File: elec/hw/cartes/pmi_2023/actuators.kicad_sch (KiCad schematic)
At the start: 0 parts

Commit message: pmi 2023 wip
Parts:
- added C27, C29, C30, C31, C32, C33, C34, C35, C36: 100nF 50V, symbol cocotter_capacitors:C_100nF_50V_0603
- added C28: 10µF 16V, symbol cocotter_capacitors:C_10µF_16V_0805
- added D2: green, 0603, symbol cocotter_diodes:green_led_0603
- added D3: yellow, 0603, symbol cocotter_diodes:yellow_led_0603
- added D4: red, 0603, symbol cocotter_diodes:red_led_0603
- added R49, R50, R51: 1k 1%, cocotter_resistor:r0603_reflow, symbol cocotter_resistors:R_1k_0603_1%
- added R87, R88, R89, R90, R91, R92, R93, R94: 0R, cocotter_resistor:r0603_reflow, symbol cocotter_resistors:R_0R_0603
- added U28: PCA9685PW, Package_SO:TSSOP-28_4.4x9.7mm_P0.65mm, symbol cocotter_ic:PCA9685PW
- added U29, U30, U31, U32: SN74LVC1T45DBV, Package_TO_SOT_SMD:SOT-23-6, symbol cocotter_ic:SN74LVC1T45DBV
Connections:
- new net: R92.2, U28.1 (A0)
- new net: R89.1, U28.2 (A1)
- new net: R94.2, U28.24 (A5)
- new net: R88.1, U28.25 (EXTCLK)
- new net: R90.1, U28.3 (A2)
- new net: R93.2, U28.4 (A3)
- new net: R91.1, U28.5 (A4)
- new net: D2.2 (A), R49.2
- new net: D4.2 (A), R51.2
- new net: D3.2 (A), R50.2
- new net +3V3: C27.1, C28.1, C29.1, C31.1, C33.1, C35.1, R49.1, R50.1, R51.1, R92.1, R93.1, R94.1, U28.28 (VDD), U29.1 (VCCA), U29.5 (DIR), U30.1 (VCCA), U30.5 (DIR), U31.1 (VCCA), U31.5 (DIR), U32.1 (VCCA), U32.5 (DIR)
- new net +5V: C30.1, C32.1, C34.1, C36.1, U29.6 (VCCB), U30.6 (VCCB), U31.6 (VCCB), U32.6 (VCCB)
- new net GND: C27.2, C28.2, C29.2, C30.2, C31.2, C32.2, C33.2, C34.2, C35.2, C36.2, R87.2, R88.2, R89.2, R90.2, R91.2, U28.14 (VSS), U29.2 (GND), U30.2 (GND), U31.2 (GND), U32.2 (GND)
- new net LED_RGB_B_3v3: U28.21 (LED14)
- new net LED_RGB_G_3v3: U28.20 (LED13)
- new net LED_RGB_R_3v3: U28.19 (LED12)
- new net LED_RGB_W_3v3: U28.22 (LED15)
- new net enable_tof_3v3: U28.13 (LED7)
- new net led_vbatt_error: D4.1 (K), U28.18 (LED11)
- new net led_vbatt_ok: D2.1 (K), U28.16 (LED9)
- new net led_vbatt_warning: D3.1 (K), U28.17 (LED10)
- new net line_led_pwm_3v3: U28.15 (LED8)
- new net scl_3v3: U28.26 (SCL)
- new net sda_3v3: U28.27 (SDA)
- new net servo_pwm_0_3v3: U28.6 (LED0), U29.3 (A)
- new net servo_pwm_0_5V: U29.4 (B)
- new net servo_pwm_1_3v3: U28.7 (LED1)
- new net servo_pwm_1_5V: U30.4 (B)
- new net servo_pwm_2_3v3: U28.8 (LED2)
- new net servo_pwm_2_5V: U31.4 (B)
- new net servo_pwm_3_3v3: U28.9 (LED3), U32.3 (A)
- new net servo_pwm_3_5V: U32.4 (B)
- new net servos_nOE: R87.1, U28.23 (~{OE})
- new net /reset_tof_3v3: U28.12 (LED6)

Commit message: pmi2023 wip
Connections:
- net pwm_vaccum_3v3: now reaches U28.11 (LED5)
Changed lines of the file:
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@@
+    (stroke (width 0) (type default))
+  )
+  (wire (pts (xy 113.03 49.53) (xy 97.79 49.53))
     (stroke (width 0) (type default))
   )
@@
     (effects (font (size 1.27 1.27)) (justify left))
   )
+  (hierarchical_label "pwm_vaccum_3v3" (shape output) (at 113.03 49.53 0) (fields_autoplaced)
+    (effects (font (size 1.27 1.27)) (justify left))
+  )

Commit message: pmi2023 wip
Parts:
- added C43 (x4): 10µF 16V, symbol cocotter_capacitors:C_10µF_16V_0805
- added J3 (x4): con_servo, symbol cocotter_connectors:con_servo
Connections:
- net +5V: now also C43.1, C43.1, C43.1, C43.1, J3.2 (5V), J3.2 (5V), J3.2 (5V), J3.2 (5V)
- net GND: now also C43.2, C43.2, C43.2, C43.2, J3.1 (GND), J3.1 (GND), J3.1 (GND), J3.1 (GND)
- net servo_pwm_0_5V: now also J3.3 (PWM)
- net servo_pwm_1_3v3: now also U30.3 (A)
- net servo_pwm_1_5V: now also J3.3 (PWM)
- net servo_pwm_2_3v3: now also U31.3 (A)
- net servo_pwm_2_5V: now also J3.3 (PWM)
- net servo_pwm_3_5V: now also J3.3 (PWM)

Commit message: pmi_2023 wip
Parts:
- C27, C29, C30, C31, C32, C33, C34, C35, C36: footprint (none) -> cocotter_capacitors:C_0603_1608Metric
- C28, C43: footprint (none) -> cocotter_capacitors:C_0805_2012Metric
- D2, D3, D4: footprint (none) -> cocotter_diodes:LED_0603_1608Metric
- J3: footprint (none) -> cocotter_connectors:ana_servo_5V
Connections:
- net led_vbatt_error: now also D4.c; no longer D4.1 (K)
- net led_vbatt_ok: now also D2.c (C); no longer D2.1 (K)
- net led_vbatt_warning: now also D3.c (C); no longer D3.1 (K)
- net at R49.2: now also D2.a (A); no longer D2.2 (A)
- net at R51.2: now also D4.a (A); no longer D4.2 (A)
- net at R50.2: now also D3.a (A); no longer D3.2 (A)
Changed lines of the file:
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@@
       (effects (font (size 1.27 1.27)) (justify left))
     )
-    (property "Footprint" "" (at 224.4852 64.77 0)
+    (property "Footprint" "cocotter_capacitors:C_0603_1608Metric" (at 224.4852 64.77 0)
       (effects (font (size 1.27 1.27)) hide)
     )
@@
       (effects (font (size 1.27 1.27)) (justify left))
     )
-    (property "Footprint" "" (at 224.4852 27.94 0)
+    (property "Footprint" "cocotter_capacitors:C_0603_1608Metric" (at 224.4852 27.94 0)
       (effects (font (size 1.27 1.27)) hide)
     )
@@
       (effects (font (size 1.27 1.27)) (justify left))
     )
-    (property "Footprint" "" (at 247.3452 48.26 0)
+    (property "Footprint" "cocotter_capacitors:C_0805_2012Metric" (at 247.3452 48.26 0)
       (effects (font (size 1.27 1.27)) hide)
     )
@@
       (effects (font (size 1.27 1.27)) (justify left))
     )
-    (property "Footprint" "" (at 247.3452 160.02 0)
+    (property "Footprint" "cocotter_capacitors:C_0805_2012Metric" (at 247.3452 160.02 0)
       (effects (font (size 1.27 1.27)) hide)
     )
@@
       (effects (font (size 1.27 1.27)))
     )
-    (property "Footprint" "" (at 265.43 114.3 0)
+    (property "Footprint" "cocotter_connectors:ana_servo_5V" (at 265.43 114.3 0)
       (effects (font (size 1.27 1.27)) hide)
     )
@@
         )
         (path "/334a657f-c66c-4260-9567-14f1c99913d7/76b412a5-2e5b-49f9-bfc4-2fef81997c2b"
-          (reference "SERVO02") (unit 1)
+          (reference "SERVO2") (unit 1)
         )
       )
@@
       (effects (font (size 1.27 1.27)) (justify left))
     )
-    (property "Footprint" "" (at 185.1152 27.94 0)
+    (property "Footprint" "cocotter_capacitors:C_0603_1608Metric" (at 185.1152 27.94 0)
       (effects (font (size 1.27 1.27)) hide)
     )
@@
       (effects (font (size 1.27 1.27)))
     )
-    (property "Footprint" "" (at 265.43 77.47 0)
+    (property "Footprint" "cocotter_connectors:ana_servo_5V" (at 265.43 77.47 0)
       (effects (font (size 1.27 1.27)) hide)
     )
@@
       (effects (font (size 1.27 1.27)) (justify left))
     )
-    (property "Footprint" "" (at 185.1152 64.77 0)
+    (property "Footprint" "cocotter_capacitors:C_0603_1608Metric" (at 185.1152 64.77 0)
       (effects (font (size 1.27 1.27)) hide)
     )
@@
       (effects (font (size 1.27 1.27)) (justify left))
     )
-    (property "Footprint" "" (at 185.1152 139.7 0)
+    (property "Footprint" "cocotter_capacitors:C_0603_1608Metric" (at 185.1152 139.7 0)
       (effects (font (size 1.27 1.27)) hide)
     )
@@
       (effects (font (size 1.27 1.27)))
     )
-    (property "Footprint" "" (at 265.43 40.64 0)
+    (property "Footprint" "cocotter_connectors:ana_servo_5V" (at 265.43 40.64 0)
       (effects (font (size 1.27 1.27)) hide)
     )
@@
       (effects (font (size 1.27 1.27)) (justify left))
     )
-    (property "Footprint" "" (at 185.1152 101.6 0)
+    (property "Footprint" "cocotter_capacitors:C_0603_1608Metric" (at 185.1152 101.6 0)
       (effects (font (size 1.27 1.27)) hide)
     )
@@
       (effects (font (size 1.27 1.27)) (justify left))
     )
-    (property "Footprint" "" (at 88.5952 29.21 0)
+    (property "Footprint" "cocotter_capacitors:C_0603_1608Metric" (at 88.5952 29.21 0)
       (effects (font (size 1.27 1.27)) hide)
     )
@@
       (effects (font (size 1.27 1.27)) hide)
     )
-    (property "Footprint" "" (at 160.02 54.61 0)
+    (property "Footprint" "cocotter_diodes:LED_0603_1608Metric" (at 160.02 54.61 0)
       (effects (font (size 1.27 1.27)) hide)
     )
@@
       (effects (font (size 1.27 1.27)) hide)
     )
-    (pin "1")
-    (pin "2")
+    (pin "a")
+    (pin "c")
     (instances
       (project "pmi_2023"
@@
       (effects (font (size 1.27 1.27)) (justify left))
     )
-    (property "Footprint" "" (at 247.3452 121.92 0)
+    (property "Footprint" "cocotter_capacitors:C_0805_2012Metric" (at 247.3452 121.92 0)
       (effects (font (size 1.27 1.27)) hide)
     )
@@
       (effects (font (size 1.27 1.27)))
     )
-    (property "Footprint" "" (at 265.43 152.4 0)
+    (property "Footprint" "cocotter_connectors:ana_servo_5V" (at 265.43 152.4 0)
       (effects (font (size 1.27 1.27)) hide)
     )
@@
       (effects (font (size 1.27 1.27)) (justify left))
     )
-    (property "Footprint" "" (at 224.4852 101.6 0)
+    (property "Footprint" "cocotter_capacitors:C_0603_1608Metric" (at 224.4852 101.6 0)
       (effects (font (size 1.27 1.27)) hide)
     )
@@
       (effects (font (size 1.27 1.27)) (justify left))
     )
-    (property "Footprint" "" (at 247.3452 85.09 0)
+    (property "Footprint" "cocotter_capacitors:C_0805_2012Metric" (at 247.3452 85.09 0)
       (effects (font (size 1.27 1.27)) hide)
     )
@@
       (effects (font (size 1.27 1.27)) (justify left))
     )
-    (property "Footprint" "" (at 106.3752 29.21 0)
+    (property "Footprint" "cocotter_capacitors:C_0805_2012Metric" (at 106.3752 29.21 0)
       (effects (font (size 1.27 1.27)) hide)
     )
@@
       (effects (font (size 1.27 1.27)) hide)
     )
-    (property "Footprint" "" (at 149.86 54.61 0)
+    (property "Footprint" "cocotter_diodes:LED_0603_1608Metric" (at 149.86 54.61 0)
       (effects (font (size 1.27 1.27)) hide)
     )
@@
       (effects (font (size 1.27 1.27)) hide)
     )
-    (pin "1")
-    (pin "2")
+    (pin "a")
+    (pin "c")
     (instances
       (project "pmi_2023"
@@
       (effects (font (size 1.27 1.27)) (justify left))
     )
-    (property "Footprint" "" (at 224.4852 139.7 0)
+    (property "Footprint" "cocotter_capacitors:C_0603_1608Metric" (at 224.4852 139.7 0)
       (effects (font (size 1.27 1.27)) hide)
     )
@@
       (effects (font (size 1.27 1.27)) hide)
     )
-    (property "Footprint" "" (at 139.7 54.61 0)
+    (property "Footprint" "cocotter_diodes:LED_0603_1608Metric" (at 139.7 54.61 0)
       (effects (font (size 1.27 1.27)) hide)
     )
@@
       (effects (font (size 1.27 1.27)) hide)
     )
-    (pin "1")
-    (pin "2")
-    (instances
-      (project "pmi_2023"
+    (pin "a")
+    (pin "c")
+    (instances
+      (project "pmi_2023"

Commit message: wip
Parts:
- removed D2: green, 0603, cocotter_diodes:LED_0603_1608Metric, symbol cocotter_diodes:green_led_0603
- removed D3: yellow, 0603, cocotter_diodes:LED_0603_1608Metric, symbol cocotter_diodes:yellow_led_0603
- removed D4: red, 0603, cocotter_diodes:LED_0603_1608Metric, symbol cocotter_diodes:red_led_0603
- added BATT_LOW1: red, 0603, cocotter_diodes:LED_0603_1608Metric, symbol cocotter_diodes:red_led_0603
- added BATT_OK1: red, 0603, cocotter_diodes:LED_0603_1608Metric, symbol cocotter_diodes:white_led_0603
- added BATT_WARN1: yellow, 0805, cocotter_diodes:LED_0805_2012Metric, symbol cocotter_diodes:yellow_led_0805
- added TP8: TestPoint, cocotter_others:testpoint-THT-0.5mm, symbol cocotter_others:TestPoint
- C13: renamed from C27; JLCPCB (none) -> C14663
- C14: renamed from C28; value 10µF 16V -> 10µF 25V; symbol cocotter_capacitors:C_10µF_16V_0805 -> cocotter_capacitors:C_10µF_16V_0805_X5R; JLCPCB (none) -> C15850; Specification 10µF 16V X7R 0805 -> 10µF 25V X5R 0805
- C15: renamed from C29; JLCPCB (none) -> C14663
- C16: renamed from C31; JLCPCB (none) -> C14663
- C17: renamed from C33; JLCPCB (none) -> C14663
- C18: renamed from C35; JLCPCB (none) -> C14663
- C19: renamed from C30; JLCPCB (none) -> C14663
- C20: renamed from C32; JLCPCB (none) -> C14663
- C21: renamed from C34; JLCPCB (none) -> C14663
- C22: renamed from C36; JLCPCB (none) -> C14663
- C23, C24, C25, C26: renamed from C43; value 10µF 16V -> 10µF 25V; symbol cocotter_capacitors:C_10µF_16V_0805 -> cocotter_capacitors:C_10µF_16V_0805_X5R; JLCPCB (none) -> C15850; Specification 10µF 16V X7R 0805 -> 10µF 25V X5R 0805
- J1, J2, J4: renamed from J3; JLCPCB (none) -> C2932698
- J3: JLCPCB (none) -> C2932698
- R54: renamed from R88; JLCPCB (none) -> C21189
- R55: renamed from R87; JLCPCB (none) -> C21189
- R56: renamed from R89; JLCPCB (none) -> C21189
- R57: renamed from R92; JLCPCB (none) -> C21189
- R58: renamed from R90; JLCPCB (none) -> C21189
- R59: renamed from R93; JLCPCB (none) -> C21189
- R60: renamed from R91; JLCPCB (none) -> C21189
- R61: renamed from R94; JLCPCB (none) -> C21189
- R62: renamed from R49; JLCPCB (none) -> C2991540; mouser 603-RC0603FR-10100KL -> (none)
- R63: renamed from R50; JLCPCB (none) -> C2991540; mouser 603-RC0603FR-10100KL -> (none)
- R64: renamed from R51; JLCPCB (none) -> C2991540; mouser 603-RC0603FR-10100KL -> (none)
- U23: renamed from U28; JLCPCB (none) -> C2678753
- U24: renamed from U29; JLCPCB (none) -> C7843
- U25: renamed from U30; JLCPCB (none) -> C7843
- U26: renamed from U31; JLCPCB (none) -> C7843
- U27: renamed from U32; JLCPCB (none) -> C7843
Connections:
- net led_vbatt_error: now also BATT_LOW1.C
- net led_vbatt_ok: now also BATT_OK1.C
- net led_vbatt_warning: now also BATT_WARN1.C
- net u23_unused_led4: now reaches U23.10 (LED4)
- net u23_unused_led4: now also TP8.1
- net at R62.2: now also BATT_OK1.A
- net at R64.2: now also BATT_LOW1.A
- net at R63.2: now also BATT_WARN1.A
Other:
- moved on the sheet: R62, R64

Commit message: wip
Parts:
- R62, R63, R64: Specification 10k 0603 1% 100mW -> 1k 0603 1% 100mW
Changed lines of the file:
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@@
       (effects (font (size 1.27 1.27)) hide)
     )
-    (property "Specification" "10k 0603 1% 100mW" (at 137.16 46.99 0)
+    (property "Specification" "1k 0603 1% 100mW" (at 137.16 46.99 0)
       (effects (font (size 1.27 1.27)) hide)
     )
@@
       (effects (font (size 1.27 1.27)) hide)
     )
-    (property "Specification" "10k 0603 1% 100mW" (at 149.86 46.99 0)
+    (property "Specification" "1k 0603 1% 100mW" (at 149.86 46.99 0)
       (effects (font (size 1.27 1.27)) hide)
     )
@@
       (effects (font (size 1.27 1.27)) hide)
     )
-    (property "Specification" "10k 0603 1% 100mW" (at 166.37 46.99 0)
-      (effects (font (size 1.27 1.27)) hide)
-    )
+    (property "Specification" "1k 0603 1% 100mW" (at 166.37 46.99 0)
+      (effects (font (size 1.27 1.27)) hide)
+    )

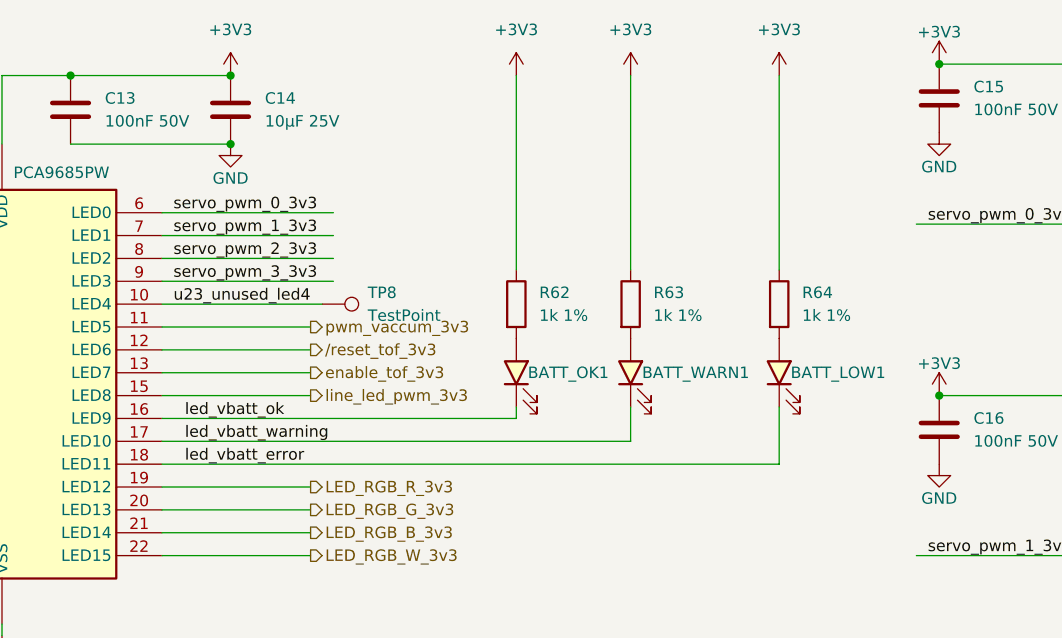
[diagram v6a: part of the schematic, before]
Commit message: pmi layout (WIP)
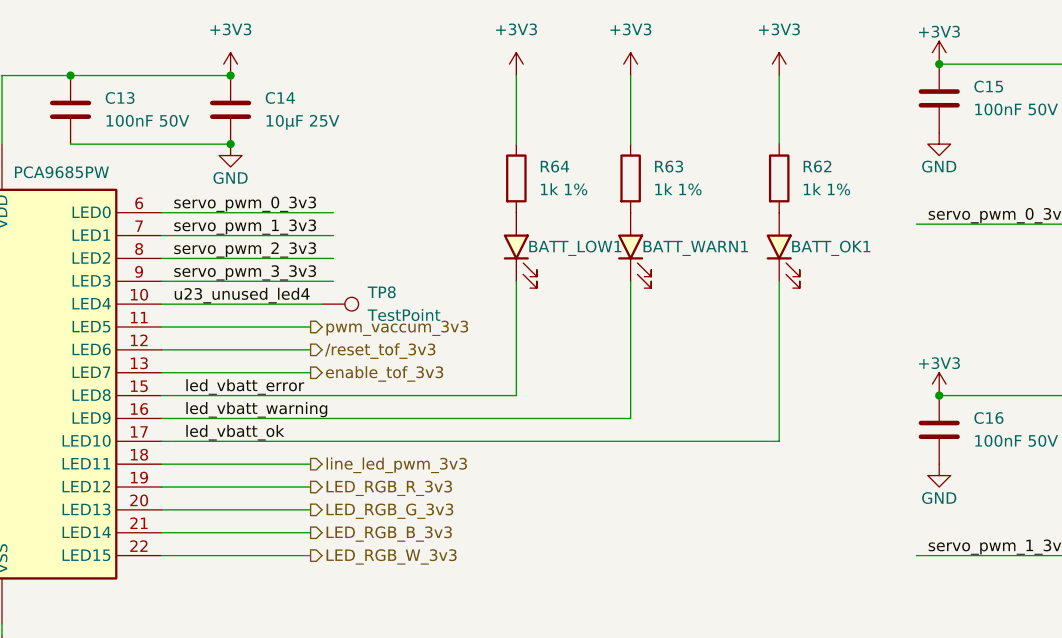
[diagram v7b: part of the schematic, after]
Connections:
- net led_vbatt_error: now also U23.15 (LED8); no longer U23.18 (LED11)
- net led_vbatt_ok: now also U23.17 (LED10); no longer U23.16 (LED9)
- net led_vbatt_warning: now also U23.16 (LED9); no longer U23.17 (LED10)
- net line_led_pwm_3v3: now also U23.18 (LED11); no longer U23.15 (LED8)
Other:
- moved on the sheet: BATT_LOW1, BATT_OK1, BATT_WARN1, R62, R63, R64

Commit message: wip
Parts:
- added D1: ~, cocotter_diodes:3528_PLCC-Reverse_mount, symbol cocotter_diodes:IN-P32TRRRGB
- added R74: 330R 1%, cocotter_resistor:r0603_reflow, symbol cocotter_resistors:R_330R_0603_1%
- added R75, R76: 51R 1%, cocotter_resistor:r0603_reflow, symbol cocotter_resistors:R_51R_0603_1%
- added TP7: TestPoint, cocotter_others:testpoint-THT-0.5mm, symbol cocotter_others:TestPoint
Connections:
- net +3V3: now also D1.4 (COM)
- net LED_RGB_B_3v3 renamed led_RGB_b_3v3
- net led_RGB_b_3v3: now also R75.1
- net LED_RGB_G_3v3 renamed led_RGB_g_3v3
- net led_RGB_g_3v3: now also R76.1
- net LED_RGB_R_3v3 renamed led_RGB_r_3v3
- net led_RGB_r_3v3: now also R74.1
- net LED_RGB_W_3v3 renamed u23_unused_led15
- net u23_unused_led15: now also TP7.1
- new net: D1.1 (C_BLUE), R75.2
- new net: D1.2 (C_GREEN), R76.2
- new net: D1.3 (C_RED), R74.2
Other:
- note added: "analog servo"
- note added: "robot color"
- moved on the sheet: C15, C16, C17, C18, C19, C20, C21, C22, C23, C24, C25, C26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
